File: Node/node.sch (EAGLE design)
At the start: 58 parts, among them J1 U.FL, U2 DW1000-I, U4 ATMEGA328, X2 332-02, Y1 8MHz

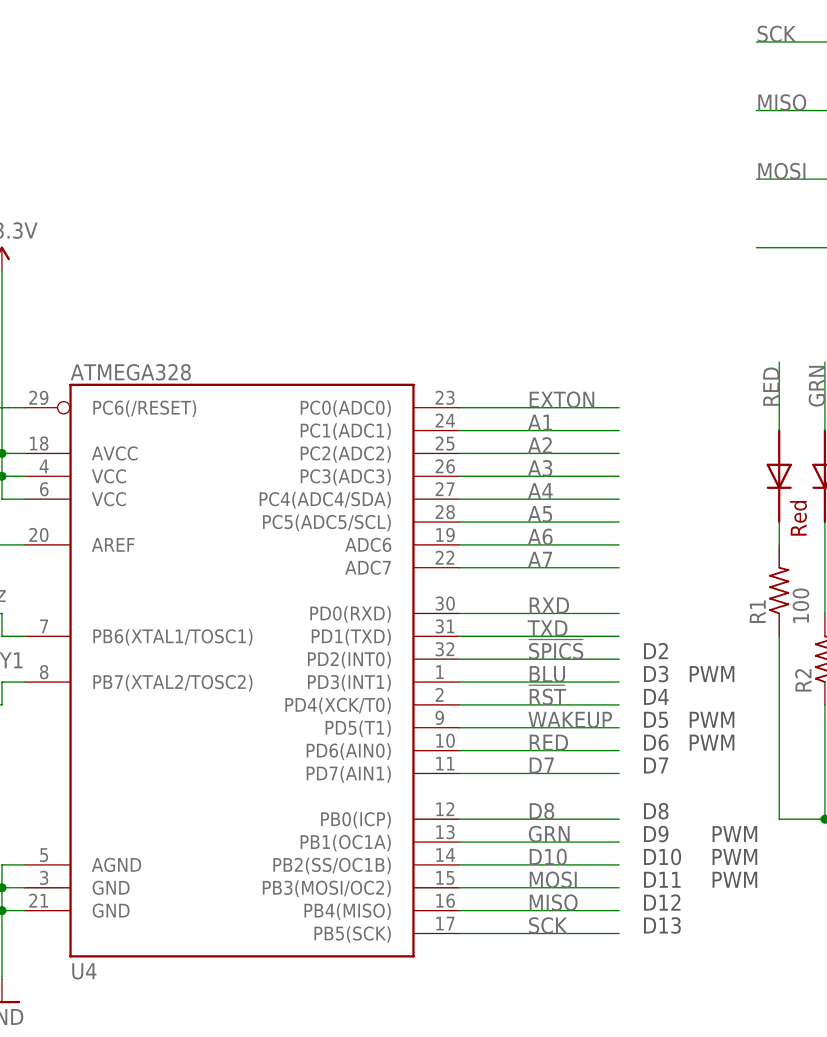
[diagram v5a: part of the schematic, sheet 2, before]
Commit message: Added IRQ to an ATMEGA Int pin, isolated !RST behind a solder bubble
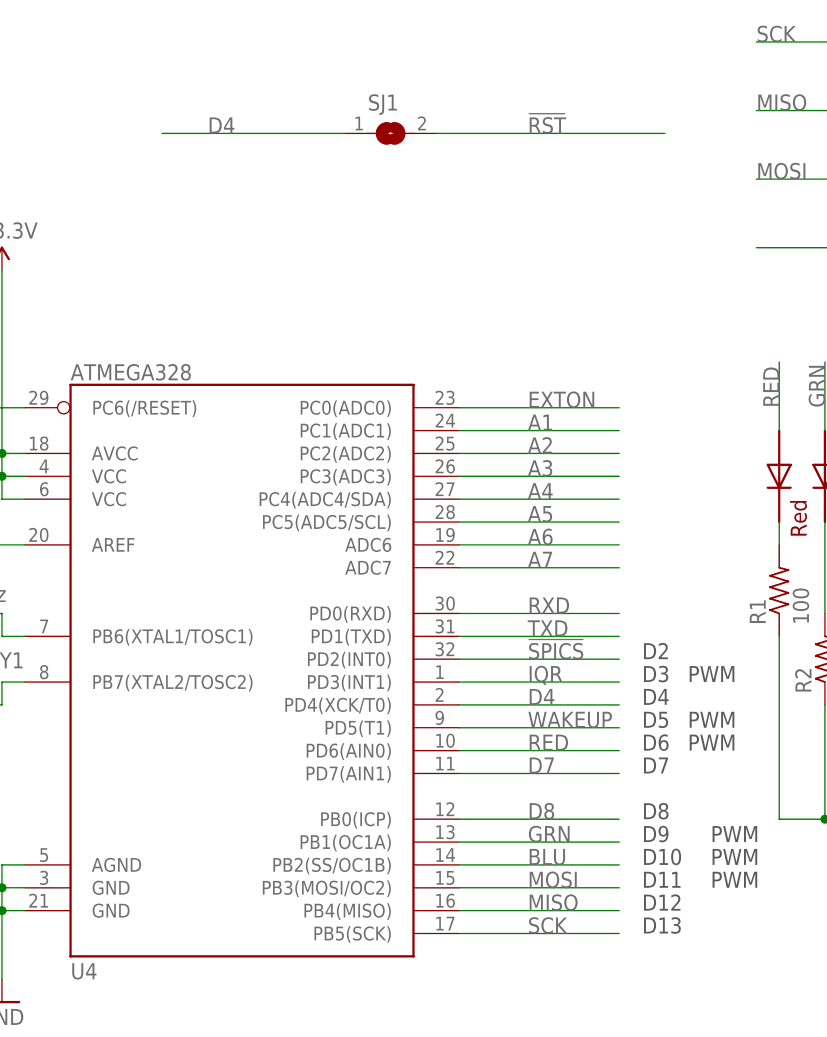
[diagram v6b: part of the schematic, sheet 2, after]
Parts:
- added SJ1: (no value), jumper:SJ
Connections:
- removed net D10: U4.PB2(SS/OC1B)
- removed net N$16: R7.2, U2.IRQ/GPIO8
- new net D4: SJ1.1, U4.PD4(XCK/T0)
- new net IQR: R7.2, U2.IRQ/GPIO8, U4.PD3(INT1)
- net !RST: now also SJ1.2; no longer U4.PD4(XCK/T0)
- net BLU: now also U4.PB2(SS/OC1B); no longer U4.PD3(INT1)
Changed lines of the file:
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@@
 <part name="U$1" library="MainLib" deviceset="5BMI-S-202-F" device=""/>
 <part name="GND16" library="SparkFun-Aesthetics" deviceset="GND" device=""/>
+<part name="SJ1" library="jumper" library_urn="urn:adsk.eagle:library:252" deviceset="SJ" device="" package3d_urn="urn:adsk.eagle:package:15471/1"/>
 </parts>
 <sheets>
@@
 <attribute name="VALUE" x="87.884" y="112.776" size="1.778" layer="96"/>
 </instance>
+<instance part="SJ1" gate="1" x="132.08" y="124.46" smashed="yes">
+<attribute name="NAME" x="129.54" y="127" size="1.778" layer="95"/>
+<attribute name="VALUE" x="129.54" y="120.65" size="1.778" layer="96"/>
+</instance>
 </instances>
 <busses>
@@
 <net name="!RST" class="0">
 <segment>
+<pinref part="SJ1" gate="1" pin="2"/>
+<wire x1="137.16" y1="124.46" x2="162.56" y2="124.46" width="0.1524" layer="91"/>
+<label x="147.32" y="124.46" size="1.778" layer="95"/>
+</segment>
+</net>
+<net name="WAKEUP" class="0">
+<segment>
+<pinref part="U4" gate="G$1" pin="PD5(T1)"/>
+<wire x1="139.7" y1="58.42" x2="157.48" y2="58.42" width="0.1524" layer="91"/>
+<label x="147.32" y="58.42" size="1.778" layer="95"/>
+</segment>
+</net>
+<net name="N$2" class="0">
+<segment>
+<pinref part="R1" gate="G$1" pin="2"/>
+<wire x1="175.26" y1="81.28" x2="175.26" y2="78.74" width="0.1524" layer="91"/>
+<pinref part="LED1" gate="G$1" pin="RED_C"/>
+</segment>
+</net>
+<net name="N$3" class="0">
+<segment>
+<pinref part="R2" gate="G$1" pin="2"/>
+<wire x1="180.34" y1="81.28" x2="180.34" y2="71.12" width="0.1524" layer="91"/>
+<pinref part="LED1" gate="G$1" pin="GREEN_C"/>
+</segment>
+</net>
+<net name="N$4" class="0">
+<segment>
+<pinref part="R3" gate="G$1" pin="2"/>
+<wire x1="185.42" y1="81.28" x2="185.42" y2="63.5" width="0.1524" layer="91"/>
+<pinref part="LED1" gate="G$1" pin="BLUE_C"/>
+</segment>
+</net>
+<net name="RED" class="0">
+<segment>
+<wire x1="175.26" y1="91.44" x2="175.26" y2="99.06" width="0.1524" layer="91"/>
+<label x="175.26" y="93.98" size="1.778" layer="95" rot="R90"/>
+<pinref part="LED1" gate="G$1" pin="RED_A"/>
+</segment>
+<segment>
+<pinref part="U4" gate="G$1" pin="PD6(AIN0)"/>
+<wire x1="139.7" y1="55.88" x2="157.48" y2="55.88" width="0.1524" layer="91"/>
+<label x="147.32" y="55.88" size="1.778" layer="95"/>
+</segment>
+</net>
+<net name="GRN" class="0">
+<segment>
+<wire x1="180.34" y1="91.44" x2="180.34" y2="99.06" width="0.1524" layer="91"/>
+<label x="180.34" y="93.98" size="1.778" layer="95" rot="R90"/>
+<pinref part="LED1" gate="G$1" pin="GREEN_A"/>
+</segment>
+<segment>
+<pinref part="U4" gate="G$1" pin="PB1(OC1A)"/>
+<wire x1="139.7" y1="45.72" x2="157.48" y2="45.72" width="0.1524" layer="91"/>
+<label x="147.32" y="45.72" size="1.778" layer="95"/>
+</segment>
+</net>
+<net name="BLU" class="0">
+<segment>
+<wire x1="185.42" y1="91.44" x2="185.42" y2="99.06" width="0.1524" layer="91"/>
+<label x="185.42" y="93.98" size="1.778" layer="95" rot="R90"/>
+<pinref part="LED1" gate="G$1" pin="BLUE_A"/>
+</segment>
+<segment>
+<pinref part="U4" gate="G$1" pin="PB2(SS/OC1B)"/>
+<wire x1="139.7" y1="43.18" x2="157.48" y2="43.18" width="0.1524" layer="91"/>
+<label x="147.32" y="43.18" size="1.778" layer="95"/>
+</segment>
+</net>
+<net name="D7" class="0">
+<segment>
+<pinref part="U4" gate="G$1" pin="PD7(AIN1)"/>
+<wire x1="139.7" y1="53.34" x2="157.48" y2="53.34" width="0.1524" layer="91"/>
+<label x="147.32" y="53.34" size="1.778" layer="95"/>
+</segment>
+</net>
+<net name="D8" class="0">
+<segment>
+<pinref part="U4" gate="G$1" pin="PB0(ICP)"/>
+<wire x1="139.7" y1="48.26" x2="157.48" y2="48.26" width="0.1524" layer="91"/>
+<label x="147.32" y="48.26" size="1.778" layer="95"/>
+</segment>
+</net>
+<net name="A6" class="0">
+<segment>
+<pinref part="U4" gate="G$1" pin="ADC6"/>
+<wire x1="139.7" y1="78.74" x2="157.48" y2="78.74" width="0.1524" layer="91"/>
+<label x="147.32" y="78.74" size="1.778" layer="95"/>
+</segment>
+</net>
+<net name="A7" class="0">
+<segment>
+<pinref part="U4" gate="G$1" pin="ADC7"/>
+<wire x1="139.7" y1="76.2" x2="157.48" y2="76.2" width="0.1524" layer="91"/>
+<label x="147.32" y="76.2" size="1.778" layer="95"/>
+</segment>
+</net>
+<net name="A3" class="0">
+<segment>
+<pinref part="U4" gate="G$1" pin="PC3(ADC3)"/>
+<wire x1="139.7" y1="86.36" x2="157.48" y2="86.36" width="0.1524" layer="91"/>
+<label x="147.32" y="86.36" size="1.778" layer="95"/>
+</segment>
+</net>
+<net name="!SPICS" class="0">
+<segment>
+<wire x1="220.98" y1="111.76" x2="172.72" y2="111.76" width="0.1524" layer="91"/>
+<label x="193.04" y="111.76" size="1.778" layer="95"/>
+</segment>
+<segment>
+<pinref part="U4" gate="G$1" pin="PD2(INT0)"/>
+<wire x1="139.7" y1="66.04" x2="157.48" y2="66.04" width="0.1524" layer="91"/>
+<label x="147.32" y="66.04" size="1.778" layer="95"/>
+</segment>
+</net>
+<net name="D4" class="0">
+<segment>
 <pinref part="U4" gate="G$1" pin="PD4(XCK/T0)"/>
 <wire x1="139.7" y1="60.96" x2="157.48" y2="60.96" width="0.1524" layer="91"/>
 <label x="147.32" y="60.96" size="1.778" layer="95"/>
 </segment>
-</net>
-<net name="WAKEUP" class="0">
-<segment>
-<pinref part="U4" gate="G$1" pin="PD5(T1)"/>
-<wire x1="139.7" y1="58.42" x2="157.48" y2="58.42" width="0.1524" layer="91"/>
-<label x="147.32" y="58.42" size="1.778" layer="95"/>
-</segment>
-</net>
-<net name="N$2" class="0">
-<segment>
-<pinref part="R1" gate="G$1" pin="2"/>
-<wire x1="175.26" y1="81.28" x2="175.26" y2="78.74" width="0.1524" layer="91"/>
-<pinref part="LED1" gate="G$1" pin="RED_C"/>
-</segment>
-</net>
-<net name="N$3" class="0">
-<segment>
-<pinref part="R2" gate="G$1" pin="2"/>
-<wire x1="180.34" y1="81.28" x2="180.34" y2="71.12" width="0.1524" layer="91"/>
-<pinref part="LED1" gate="G$1" pin="GREEN_C"/>
-</segment>
-</net>
-<net name="N$4" class="0">
-<segment>
-<pinref part="R3" gate="G$1" pin="2"/>
-<wire x1="185.42" y1="81.28" x2="185.42" y2="63.5" width="0.1524" layer="91"/>
-<pinref part="LED1" gate="G$1" pin="BLUE_C"/>
-</segment>
-</net>
-<net name="RED" class="0">
-<segment>
-<wire x1="175.26" y1="91.44" x2="175.26" y2="99.06" width="0.1524" layer="91"/>
-<label x="175.26" y="93.98" size="1.778" layer="95" rot="R90"/>
-<pinref part="LED1" gate="G$1" pin="RED_A"/>
-</segment>
-<segment>
-<pinref part="U4" gate="G$1" pin="PD6(AIN0)"/>
-<wire x1="139.7" y1="55.88" x2="157.48" y2="55.88" width="0.1524" layer="91"/>
-<label x="147.32" y="55.88" size="1.778" layer="95"/>
-</segment>
-</net>
-<net name="GRN" class="0">
-<segment>
-<wire x1="180.34" y1="91.44" x2="180.34" y2="99.06" width="0.1524" layer="91"/>
-<label x="180.34" y="93.98" size="1.778" layer="95" rot="R90"/>
-<pinref part="LED1" gate="G$1" pin="GREEN_A"/>
-</segment>
-<segment>
-<pinref part="U4" gate="G$1" pin="PB1(OC1A)"/>
-<wire x1="139.7" y1="45.72" x2="157.48" y2="45.72" width="0.1524" layer="91"/>
-<label x="147.32" y="45.72" size="1.778" layer="95"/>
-</segment>
-</net>
-<net name="BLU" class="0">
-<segment>
-<wire x1="185.42" y1="91.44" x2="185.42" y2="99.06" width="0.1524" layer="91"/>
-<label x="185.42" y="93.98" size="1.778" layer="95" rot="R90"/>
-<pinref part="LED1" gate="G$1" pin="BLUE_A"/>
-</segment>
+<segment>
+<pinref part="SJ1" gate="1" pin="1"/>
+<wire x1="127" y1="124.46" x2="106.68" y2="124.46" width="0.1524" layer="91"/>
+<label x="111.76" y="124.46" size="1.778" layer="95"/>
+</segment>
+</net>
+<net name="IQR" class="0">
 <segment>
 <pinref part="U4" gate="G$1" pin="PD3(INT1)"/>
 <wire x1="139.7" y1="63.5" x2="157.48" y2="63.5" width="0.1524" layer="91"/>
 <label x="147.32" y="63.5" size="1.778" layer="95"/>
-</segment>
-</net>
-<net name="D7" class="0">
-<segment>
-<pinref part="U4" gate="G$1" pin="PD7(AIN1)"/>
-<wire x1="139.7" y1="53.34" x2="157.48" y2="53.34" width="0.1524" layer="91"/>
-<label x="147.32" y="53.34" size="1.778" layer="95"/>
-</segment>
-</net>
-<net name="D8" class="0">
-<segment>
-<pinref part="U4" gate="G$1" pin="PB0(ICP)"/>
-<wire x1="139.7" y1="48.26" x2="157.48" y2="48.26" width="0.1524" layer="91"/>
-<label x="147.32" y="48.26" size="1.778" layer="95"/>
-</segment>
-</net>
-<net name="A6" class="0">
-<segment>
-<pinref part="U4" gate="G$1" pin="ADC6"/>
-<wire x1="139.7" y1="78.74" x2="157.48" y2="78.74" width="0.1524" layer="91"/>
-<label x="147.32" y="78.74" size="1.778" layer="95"/>
-</segment>
-</net>
-<net name="A7" class="0">
-<segment>
-<pinref part="U4" gate="G$1" pin="ADC7"/>
-<wire x1="139.7" y1="76.2" x2="157.48" y2="76.2" width="0.1524" layer="91"/>
-<label x="147.32" y="76.2" size="1.778" layer="95"/>
-</segment>
-</net>
-<net name="A3" class="0">
-<segment>
-<pinref part="U4" gate="G$1" pin="PC3(ADC3)"/>
-<wire x1="139.7" y1="86.36" x2="157.48" y2="86.36" width="0.1524" layer="91"/>
-<label x="147.32" y="86.36" size="1.778" layer="95"/>
-</segment>
-</net>
-<net name="D10" class="0">
-<segment>
-<pinref part="U4" gate="G$1" pin="PB2(SS/OC1B)"/>
-<wire x1="139.7" y1="43.18" x2="157.48" y2="43.18" width="0.1524" layer="91"/>
-<label x="147.32" y="43.18" size="1.778" layer="95"/>
-</segment>
-</net>
-<net name="!SPICS" class="0">
-<segment>
-<wire x1="220.98" y1="111.76" x2="172.72" y2="111.76" width="0.1524" layer="91"/>
-<label x="193.04" y="111.76" size="1.778" layer="95"/>
-</segment>
-<segment>
-<pinref part="U4" gate="G$1" pin="PD2(INT0)"/>
-<wire x1="139.7" y1="66.04" x2="157.48" y2="66.04" width="0.1524" layer="91"/>
-<label x="147.32" y="66.04" size="1.778" layer="95"/>
 </segment>
 </net>
@@
 </segment>
 </net>
-<net name="N$16" class="0">
+<net name="IQR" class="0">
 <segment>
 <pinref part="U2" gate="G$1" pin="IRQ/GPIO8"/>
 <wire x1="162.56" y1="60.96" x2="193.04" y2="60.96" width="0.1524" layer="91"/>
 <pinref part="R7" gate="G$1" pin="2"/>
-</segment>
-</net>
+<label x="177.8" y="60.96" size="1.778" layer="95"/>
+</segment>
+</net>

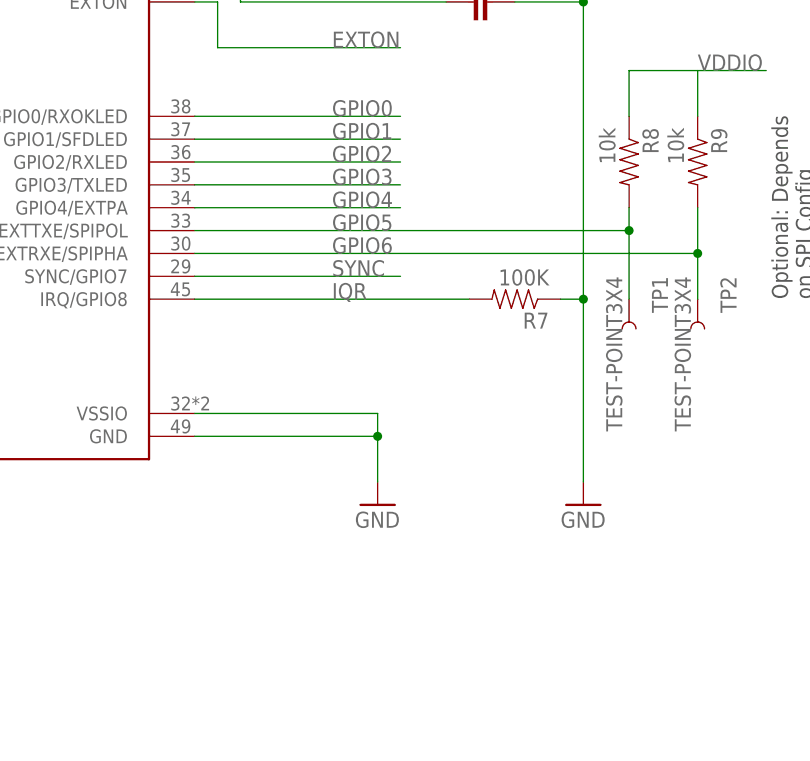
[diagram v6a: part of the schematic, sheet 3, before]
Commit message: Added TX and RX leds for the DW1000
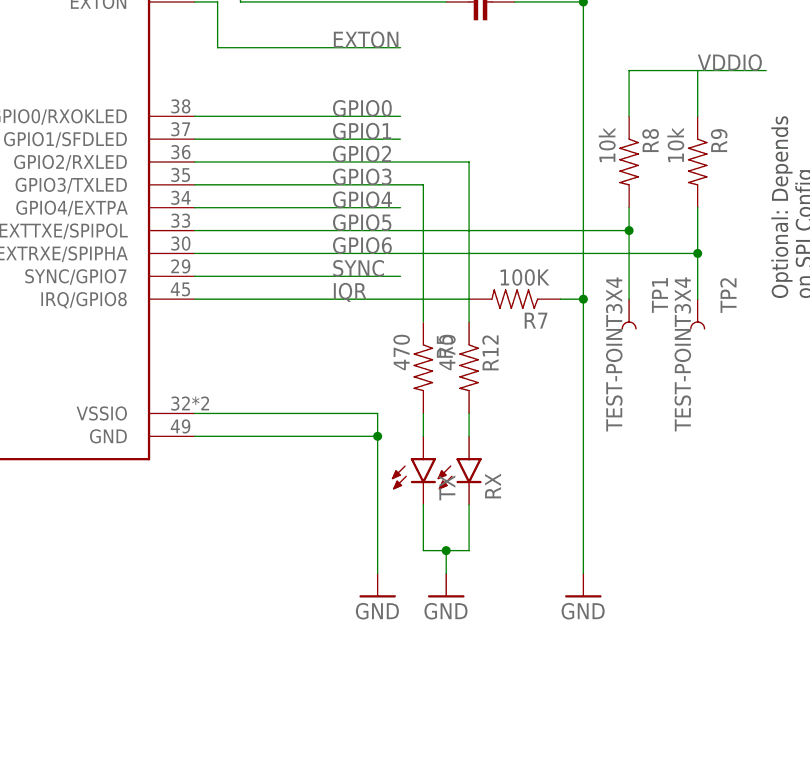
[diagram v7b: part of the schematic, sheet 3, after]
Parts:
- added R12, R5: 470, SparkFun-Passives:RESISTOR0805-RES
- added RX, TX: (no value), SparkFun-LED:LED0603
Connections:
- new net N$5: R5.2, TX.A
- new net N$6: R12.2, RX.A
- net GND: now also RX.C, TX.C
- net GPIO2: now also R12.1
- net GPIO3: now also R5.1
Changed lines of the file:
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@@
 <part name="GND16" library="SparkFun-Aesthetics" deviceset="GND" device=""/>
 <part name="SJ1" library="jumper" library_urn="urn:adsk.eagle:library:252" deviceset="SJ" device="" package3d_urn="urn:adsk.eagle:package:15471/1"/>
+<part name="TX" library="SparkFun-LED" deviceset="LED" device="0603"/>
+<part name="RX" library="SparkFun-LED" deviceset="LED" device="0603"/>
+<part name="R5" library="SparkFun-Passives" deviceset="RESISTOR" device="0805-RES" value="470"/>
+<part name="R12" library="SparkFun-Passives" deviceset="RESISTOR" device="0805-RES" value="470"/>
+<part name="GND12" library="SparkFun-Aesthetics" deviceset="GND" device=""/>
 </parts>
 <sheets>
@@
 <attribute name="VALUE" x="116.8066" y="40.5482" size="1.78091875" layer="96" ratio="10"/>
 </instance>
-<instance part="GND3" gate="1" x="182.88" y="38.1" smashed="yes">
-<attribute name="VALUE" x="180.34" y="35.56" size="1.778" layer="96"/>
+<instance part="GND3" gate="1" x="182.88" y="27.94" smashed="yes">
+<attribute name="VALUE" x="180.34" y="25.4" size="1.778" layer="96"/>
 </instance>
 <instance part="R6" gate="G$1" x="101.6" y="76.2" smashed="yes">
@@
 <attribute name="VALUE" x="194.691" y="150.876" size="1.778" layer="96" rot="R90"/>
 </instance>
-<instance part="GND5" gate="1" x="205.74" y="38.1" smashed="yes">
-<attribute name="VALUE" x="203.2" y="35.56" size="1.778" layer="96"/>
+<instance part="GND5" gate="1" x="205.74" y="27.94" smashed="yes">
+<attribute name="VALUE" x="203.2" y="25.4" size="1.778" layer="96"/>
 </instance>
 <instance part="BALUN1" gate="G$1" x="50.8" y="91.44" smashed="yes">
@@
 <instance part="GND16" gate="1" x="38.1" y="15.24" smashed="yes">
 <attribute name="VALUE" x="35.56" y="12.7" size="1.778" layer="96"/>
+</instance>
+<instance part="TX" gate="G$1" x="187.96" y="43.18" smashed="yes">
+<attribute name="NAME" x="191.516" y="38.608" size="1.778" layer="95" rot="R90"/>
+<attribute name="VALUE" x="193.675" y="38.608" size="1.778" layer="96" rot="R90"/>
+</instance>
+<instance part="RX" gate="G$1" x="193.04" y="43.18" smashed="yes">
+<attribute name="NAME" x="196.596" y="38.608" size="1.778" layer="95" rot="R90"/>
+<attribute name="VALUE" x="198.755" y="38.608" size="1.778" layer="96" rot="R90"/>
+</instance>
+<instance part="R5" gate="G$1" x="187.96" y="53.34" smashed="yes" rot="R270">
+<attribute name="NAME" x="189.4586" y="57.15" size="1.778" layer="95" rot="R270"/>
+<attribute name="VALUE" x="184.658" y="57.15" size="1.778" layer="96" rot="R270"/>
+</instance>
+<instance part="R12" gate="G$1" x="193.04" y="53.34" smashed="yes" rot="R270">
+<attribute name="NAME" x="194.5386" y="57.15" size="1.778" layer="95" rot="R270"/>
+<attribute name="VALUE" x="189.738" y="57.15" size="1.778" layer="96" rot="R270"/>
+</instance>
+<instance part="GND12" gate="1" x="190.5" y="27.94" smashed="yes">
+<attribute name="VALUE" x="187.96" y="25.4" size="1.778" layer="96"/>
 </instance>
 </instances>
@@
 <segment>
 <pinref part="GND3" gate="1" pin="GND"/>
-<wire x1="182.88" y1="40.64" x2="182.88" y2="45.72" width="0.1524" layer="91"/>
+<wire x1="182.88" y1="30.48" x2="182.88" y2="45.72" width="0.1524" layer="91"/>
 <pinref part="U2" gate="G$1" pin="GND"/>
 <wire x1="162.56" y1="45.72" x2="182.88" y2="45.72" width="0.1524" layer="91"/>
@@
 <wire x1="205.74" y1="99.06" x2="205.74" y2="93.98" width="0.1524" layer="91"/>
 <wire x1="205.74" y1="93.98" x2="205.74" y2="60.96" width="0.1524" layer="91"/>
-<wire x1="205.74" y1="60.96" x2="205.74" y2="40.64" width="0.1524" layer="91"/>
+<wire x1="205.74" y1="60.96" x2="205.74" y2="30.48" width="0.1524" layer="91"/>
 <wire x1="193.04" y1="149.86" x2="205.74" y2="149.86" width="0.1524" layer="91"/>
 <wire x1="205.74" y1="149.86" x2="205.74" y2="139.7" width="0.1524" layer="91"/>
@@
 </segment>
 <segment>
+<pinref part="GND16" gate="1" pin="GND"/>
 <pinref part="U$1" gate="G$1" pin="P$1"/>
-<pinref part="GND16" gate="1" pin="GND"/>
 <wire x1="38.1" y1="22.86" x2="38.1" y2="17.78" width="0.1524" layer="91"/>
+</segment>
+<segment>
+<pinref part="TX" gate="G$1" pin="C"/>
+<wire x1="187.96" y1="38.1" x2="187.96" y2="33.02" width="0.1524" layer="91"/>
+<pinref part="RX" gate="G$1" pin="C"/>
+<wire x1="187.96" y1="33.02" x2="190.5" y2="33.02" width="0.1524" layer="91"/>
+<wire x1="190.5" y1="33.02" x2="193.04" y2="33.02" width="0.1524" layer="91"/>
+<wire x1="193.04" y1="33.02" x2="193.04" y2="38.1" width="0.1524" layer="91"/>
+<pinref part="GND12" gate="1" pin="GND"/>
+<wire x1="190.5" y1="33.02" x2="190.5" y2="30.48" width="0.1524" layer="91"/>
+<junction x="190.5" y="33.02"/>
 </segment>
 </net>
@@
 <segment>
 <pinref part="U2" gate="G$1" pin="GPIO2/RXLED"/>
-<wire x1="162.56" y1="76.2" x2="185.42" y2="76.2" width="0.1524" layer="91"/>
+<wire x1="162.56" y1="76.2" x2="193.04" y2="76.2" width="0.1524" layer="91"/>
 <label x="177.8" y="76.2" size="1.778" layer="95"/>
+<pinref part="R12" gate="G$1" pin="1"/>
+<wire x1="193.04" y1="76.2" x2="193.04" y2="58.42" width="0.1524" layer="91"/>
 </segment>
 </net>
@@
 <segment>
 <pinref part="U2" gate="G$1" pin="GPIO3/TXLED"/>
-<wire x1="162.56" y1="73.66" x2="185.42" y2="73.66" width="0.1524" layer="91"/>
+<wire x1="162.56" y1="73.66" x2="187.96" y2="73.66" width="0.1524" layer="91"/>
 <label x="177.8" y="73.66" size="1.778" layer="95"/>
+<pinref part="R5" gate="G$1" pin="1"/>
+<wire x1="187.96" y1="73.66" x2="187.96" y2="58.42" width="0.1524" layer="91"/>
 </segment>
 </net>
@@
 </segment>
 </net>
+<net name="N$5" class="0">
+<segment>
+<pinref part="TX" gate="G$1" pin="A"/>
+<pinref part="R5" gate="G$1" pin="2"/>
+<wire x1="187.96" y1="45.72" x2="187.96" y2="48.26" width="0.1524" layer="91"/>
+</segment>
+</net>
+<net name="N$6" class="0">
+<segment>
+<pinref part="RX" gate="G$1" pin="A"/>
+<pinref part="R12" gate="G$1" pin="2"/>
+<wire x1="193.04" y1="45.72" x2="193.04" y2="48.26" width="0.1524" layer="91"/>
+</segment>
+</net>
